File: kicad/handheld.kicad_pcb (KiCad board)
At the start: 4 copper layers, 240 x 76 mm, 95 parts, among them J1 Conn_01x08, J2 61300311121, J3 AVR-PDI-6, J4 UE27AC54100, SW1 HOLD, SW2 PAUSE, SW3 SDROP, SW4 HDROP, SW5 ROTR, SW6 RIGHT, SW7 ROTL, SW8 RIGHT, U1 TFBS4711, U10 DMN601, U11 NSI45015, U12 SN54LV574, U13 P-FET, U14 NSI45015, U15 DMN601, U16 NSI45015, U17 NSI45015, U18 DMN601, U19 P-FET, U2 ATxmega64C3-AU, U20 NSI45015, U21 74HCT595, U22 NSI45015, U23 DMN601, U24 NSI45015, U25 P-FET, U26 NSI45015, U27 DMN601, U28 NSI45015, U29 SN54LV574, U3 P-FET, U30 NSI45015, U31 DMN601, U32 NSI45015, U33 P-FET, U34 NSI45015, U35 DMN601, U36 NSI45015, U37 NSI45015, U38 P-FET, U39 DMN601, U4 LM3671MF-3.3, U40 NSI45015, U41 NSI45015, U42 DMN601, U43 NSI45015, U44 SN54LV574, U45 74HCT595, U46 P-FET, U47 NSI45015, U48 DMN601, U49 NSI45015, U5 NSI45015, U50 NSI45015, U51 DMN601, U52 P-FET, U53 NSI45015, U6 P-FET, U7 DMN601, U8 NSI45015, U9 NSI45015

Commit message: First stab at constant current drivers
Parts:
- moved U9 232.2 mm to (122.4, 117.6), turned to 180 degrees
- moved U5 229.1 mm to (122.4, 120.6), turned to 180 degrees
- moved U17 226.7 mm to (122.4, 111.6), turned to 180 degrees
- moved U8 221.2 mm to (133.4, 120.6), turned to 180 degrees
- moved U16 206.8 mm to (133.4, 114.6), turned to 180 degrees
- moved U11 205.5 mm to (133.4, 117.6), turned to 180 degrees
- moved U20 204.5 mm to (133.4, 111.6), turned to 180 degrees
- moved U14 195.4 mm to (122.4, 114.6), turned to 180 degrees
- moved C7 190.2 mm to (149.5, 128.3), turned to 180 degrees
- moved C10 187.7 mm to (192.6, 90.3), turned to 180 degrees
- moved C8 155.1 mm to (192.5, 128.3), turned to 180 degrees
- moved U36 147.0 mm to (193.4, 151.6), turned to 180 degrees
- moved U24 140.3 mm to (210.0, 161.3), turned to 180 degrees
- moved U30 128.6 mm to (229.1, 161.3), turned to 180 degrees
- moved U22 127.4 mm to (203.7, 161.3), turned to 180 degrees
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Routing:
- net /Matrix Driver/COL3: track 0.00 -> 63.2 mm, vias 0 -> 1
- net /Matrix Driver/COL5: track 0.00 -> 61.6 mm, vias 0 -> 1
- net /Matrix Driver/COL1: track 0.00 -> 61.4 mm, vias 0 -> 1
- net /Matrix Driver/COL0: track 0.00 -> 60.8 mm, vias 0 -> 1
- net /Matrix Driver/COL6: track 0.00 -> 59.6 mm, vias 0 -> 1
- net /Matrix Driver/COL2: track 0.00 -> 48.3 mm, vias 0 -> 1
- net /Matrix Driver/COL4: track 0.00 -> 43.4 mm, vias 0 -> 1
- net /Matrix Driver/COL7: track 0.00 -> 34.9 mm, vias 0 -> 1
- net Net-(U5-Pad1): track 0.00 -> 22.3 mm
- net Net-(U10-Pad6): track 0.00 -> 20.1 mm
- net Net-(U17-Pad1): track 0.00 -> 19.4 mm
- net Net-(U14-Pad1): track 0.00 -> 19.1 mm
- net /Matrix Driver/ROW9: track 97.6 -> 114.2 mm, vias 2 -> 3
- net Net-(U39-Pad2): track 0.00 -> 13.4 mm
- net Net-(U42-Pad2): track 0.00 -> 12.6 mm
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
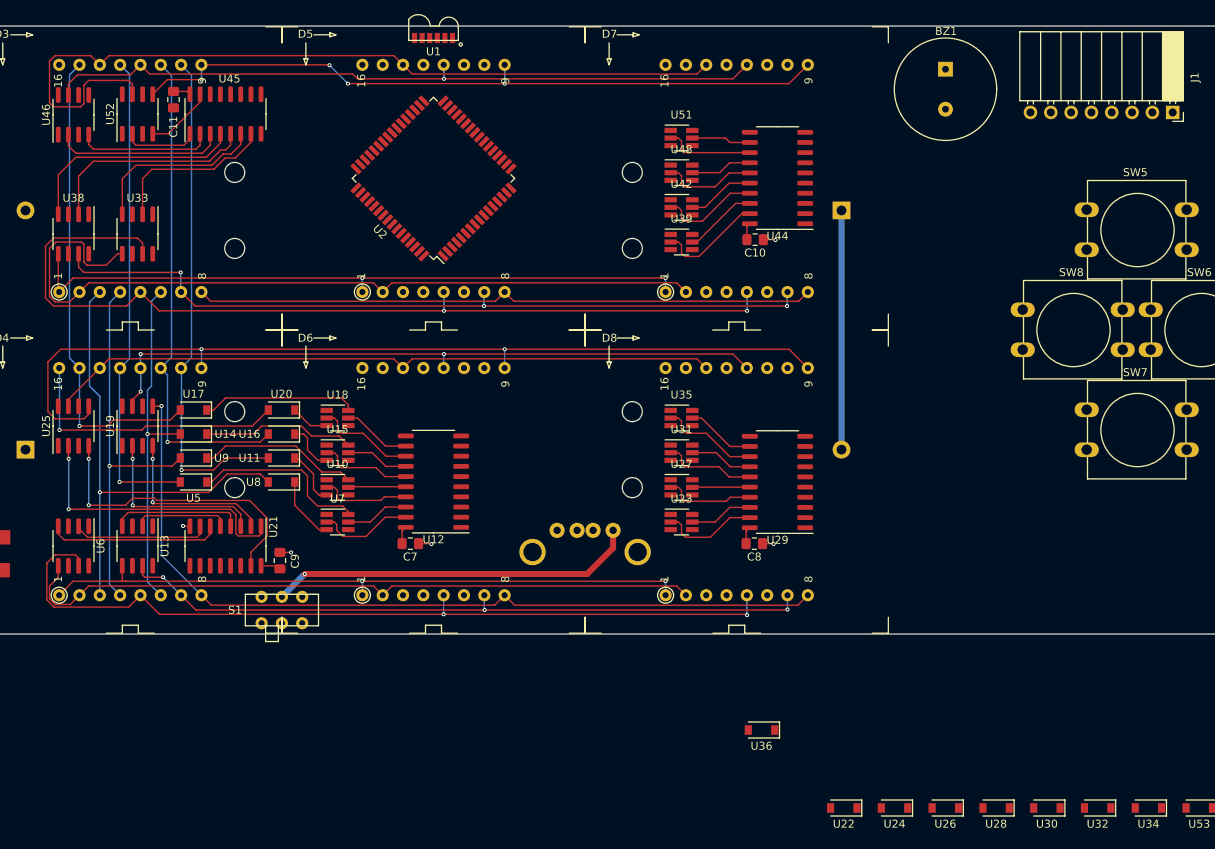
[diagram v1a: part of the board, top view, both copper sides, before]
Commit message: Adds more constant current drivers
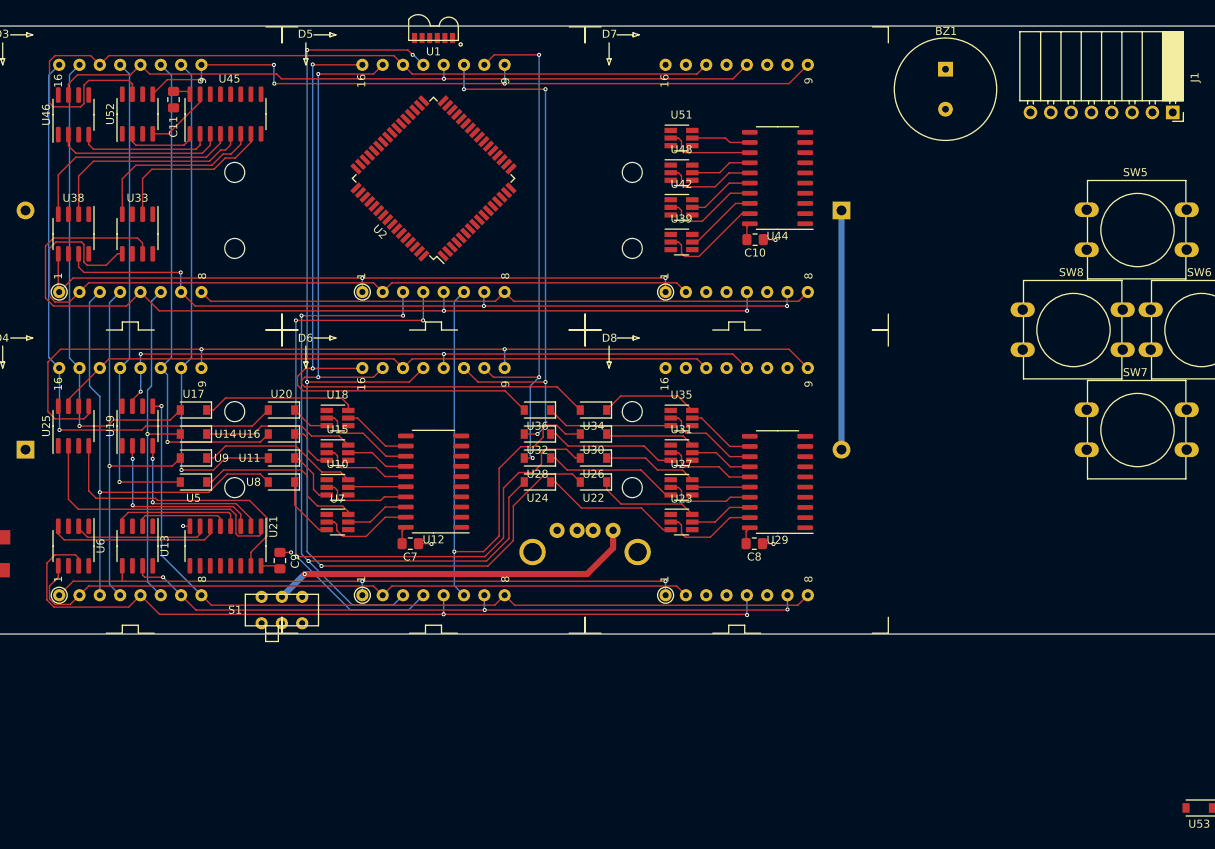
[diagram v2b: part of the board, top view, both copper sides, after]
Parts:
- moved U34 85.4 mm to (172.4, 111.6)
- moved U32 84.2 mm to (165.4, 114.6)
- moved U30 73.5 mm to (172.4, 114.6)
- moved U28 72.1 mm to (165.4, 117.6)
- moved U26 62.0 mm to (172.4, 117.6)
- moved U24 60.4 mm to (165.4, 120.6)
- moved U22 51.4 mm to (172.4, 120.6)
- moved U36 48.8 mm to (165.4, 111.6)
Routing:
- net /Matrix Driver/COL8: track 0.00 -> 135.9 mm, vias 0 -> 4
- net /Matrix Driver/COL10: track 0.00 -> 114.3 mm, vias 0 -> 3
- net /Matrix Driver/COL9: track 0.00 -> 95.4 mm, vias 0 -> 3
- net /Matrix Driver/COL14: track 0.00 -> 93.8 mm, vias 0 -> 2
- net /Matrix Driver/COL15: track 0.00 -> 83.5 mm, vias 0 -> 2
- net /Matrix Driver/COL13: track 0.00 -> 69.3 mm, vias 0 -> 4
- net /Matrix Driver/COL12: track 0.00 -> 67.3 mm, vias 0 -> 1
- net /Matrix Driver/COL11: track 0.00 -> 66.7 mm, vias 0 -> 3
- net /Matrix Driver/COL7: track 34.9 -> 73.9 mm
- net Net-(U23-Pad3): track 0.00 -> 17.5 mm
- net Net-(U27-Pad3): track 0.00 -> 16.9 mm
- net Net-(U31-Pad3): track 0.00 -> 16.4 mm
- net Net-(U35-Pad3): track 0.00 -> 15.8 mm
- net Net-(U22-Pad1): track 0.00 -> 12.9 mm
- net Net-(U34-Pad1): track 0.00 -> 12.2 mm
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
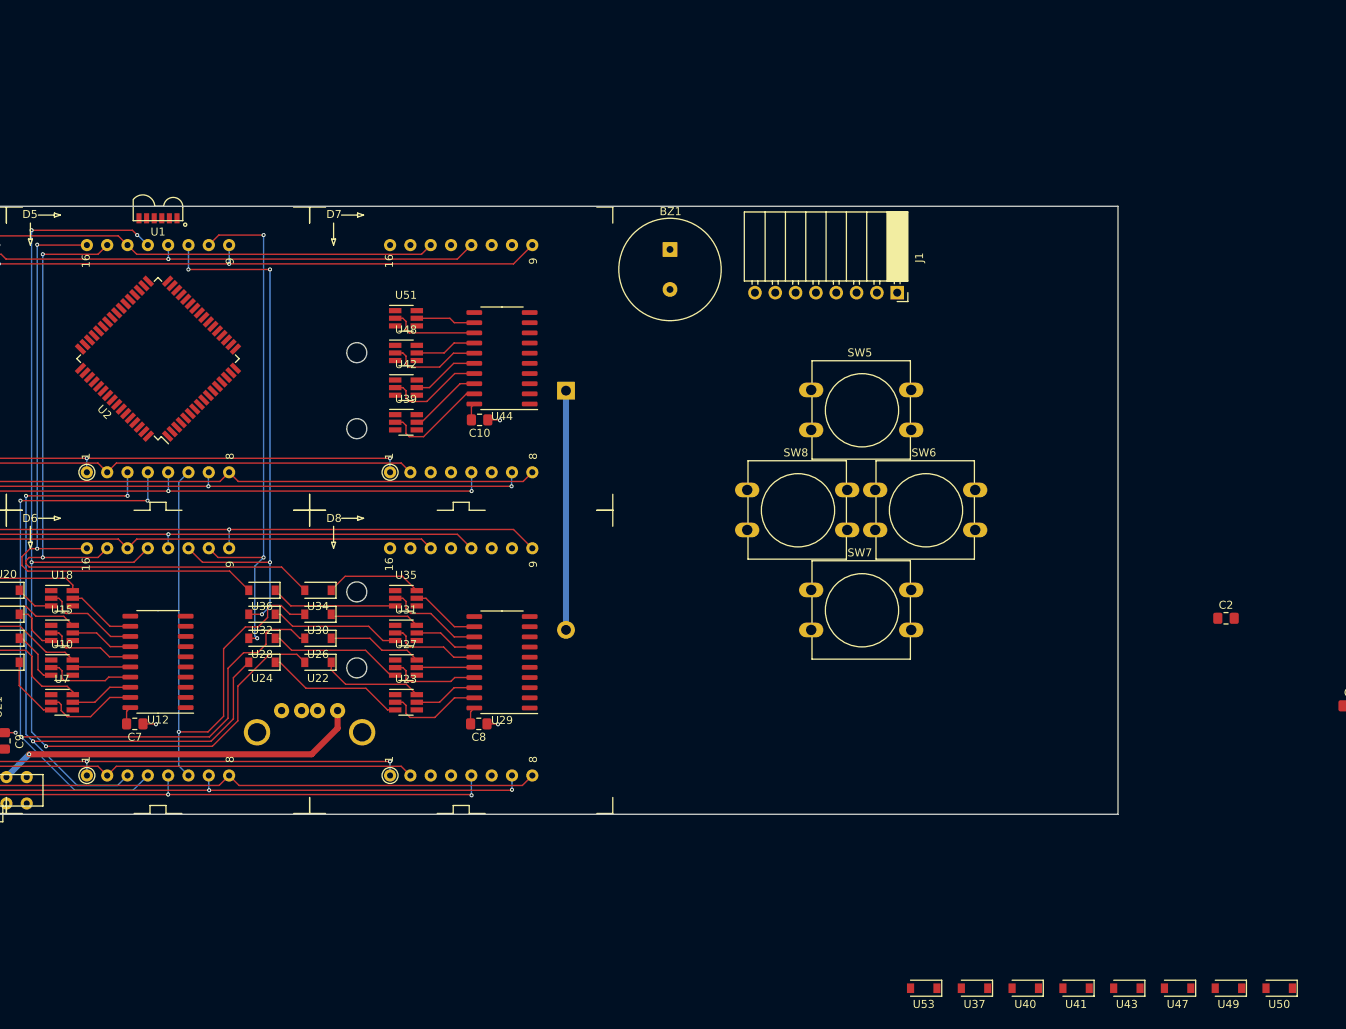
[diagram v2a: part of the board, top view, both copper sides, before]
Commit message: Adds more column circuitry
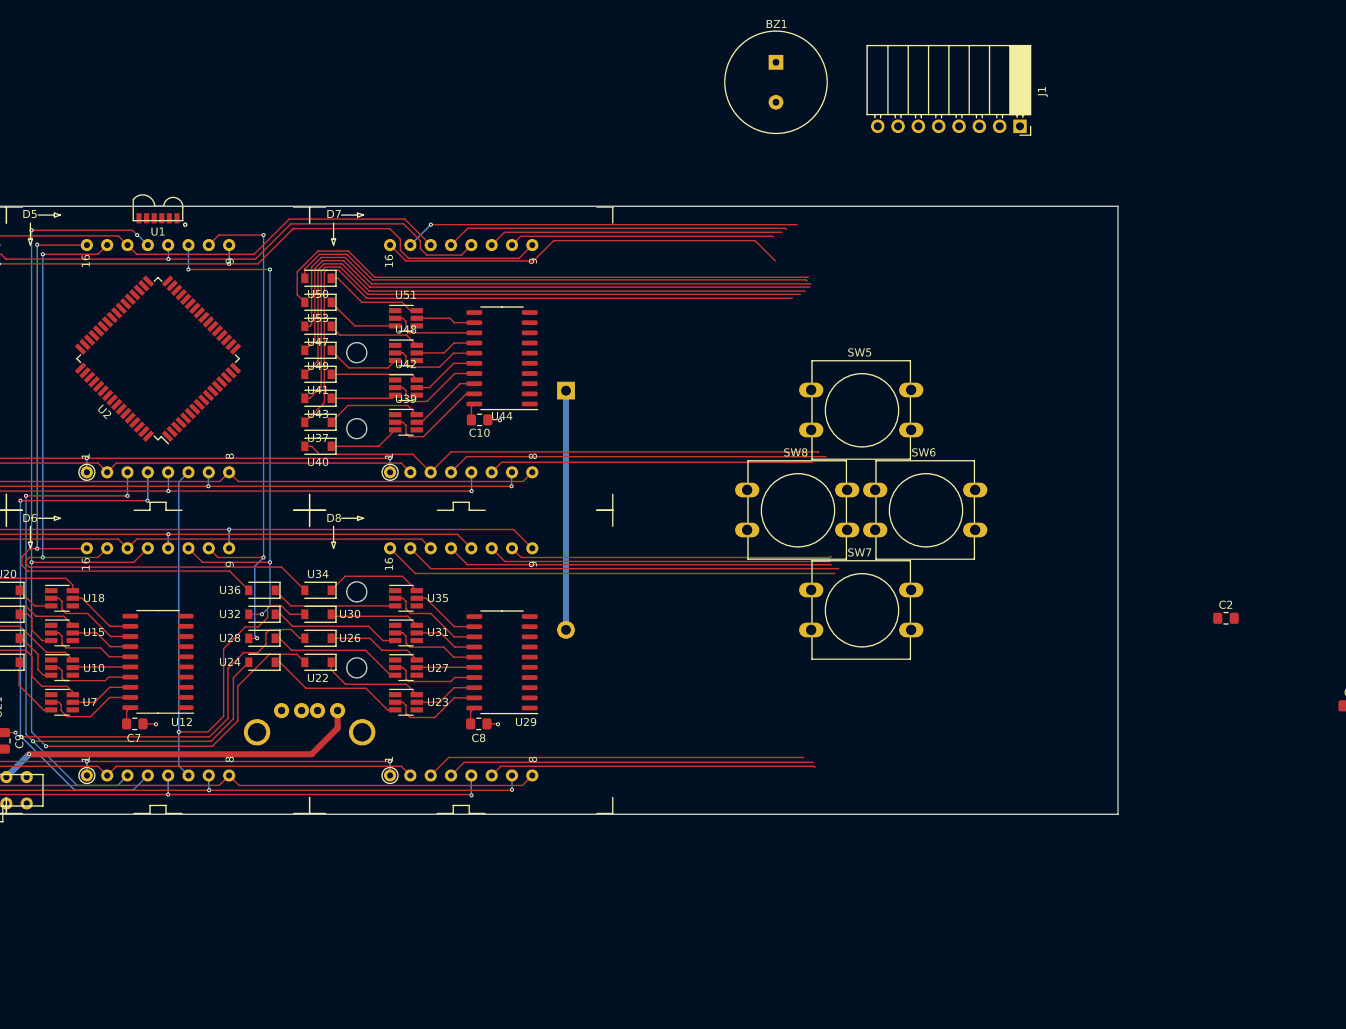
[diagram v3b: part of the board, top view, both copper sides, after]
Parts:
- moved U50 149.4 mm to (172.4, 72.6)
- moved U49 139.0 mm to (172.4, 81.6)
- moved U47 135.6 mm to (172.4, 78.6)
- moved U43 125.1 mm to (172.4, 87.6)
- moved U41 121.9 mm to (172.4, 84.6)
- moved U53 114.4 mm to (172.4, 75.6)
- moved U40 111.4 mm to (172.4, 93.6)
- moved U37 108.3 mm to (172.4, 90.6)
- moved BZ1 26.9 mm to (229.7, 45.6)
- moved J1 25.9 mm to (260.1, 53.6)
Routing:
- net /Matrix Driver/COL23: track 0.00 -> 178.5 mm
- net /Matrix Driver/COL16: track 0.00 -> 171.1 mm
- net /Matrix Driver/COL22: track 0.00 -> 170.1 mm, vias 0 -> 1
- net /Matrix Driver/COL18: track 0.00 -> 170.0 mm
- net /Matrix Driver/COL21: track 0.00 -> 154.3 mm
- net /Matrix Driver/COL20: track 0.00 -> 154.0 mm
- net /Matrix Driver/COL19: track 0.00 -> 152.2 mm
- net /Matrix Driver/COL17: track 0.00 -> 114.2 mm
- net Net-(U50-Pad1): track 0.00 -> 12.4 mm
- net Net-(U37-Pad1): track 0.00 -> 12.0 mm
- net Net-(U47-Pad1): track 0.00 -> 11.7 mm
- net Net-(U41-Pad1): track 0.00 -> 11.0 mm
- net Net-(U48-Pad3): track 0.00 -> 9.29 mm
- net Net-(U51-Pad3): track 0.00 -> 9.22 mm
- net Net-(U39-Pad3): track 0.00 -> 8.85 mm
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
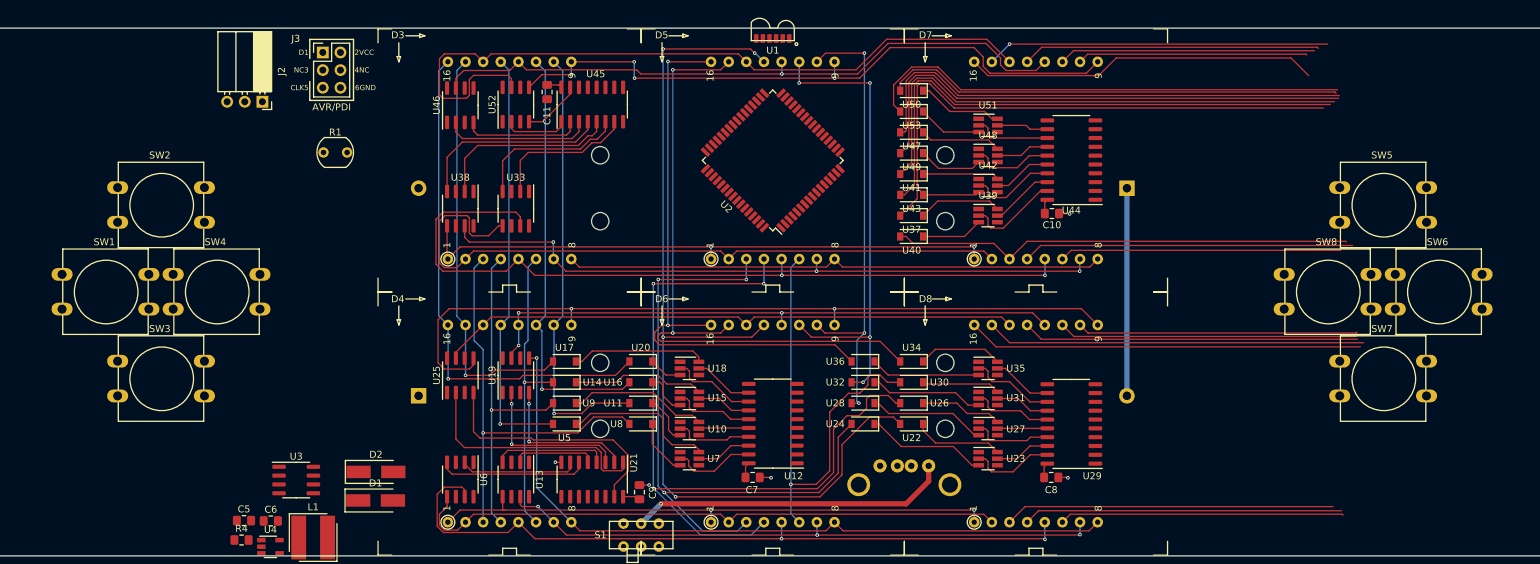
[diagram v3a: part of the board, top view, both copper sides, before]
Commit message: Wires up USB and buttons
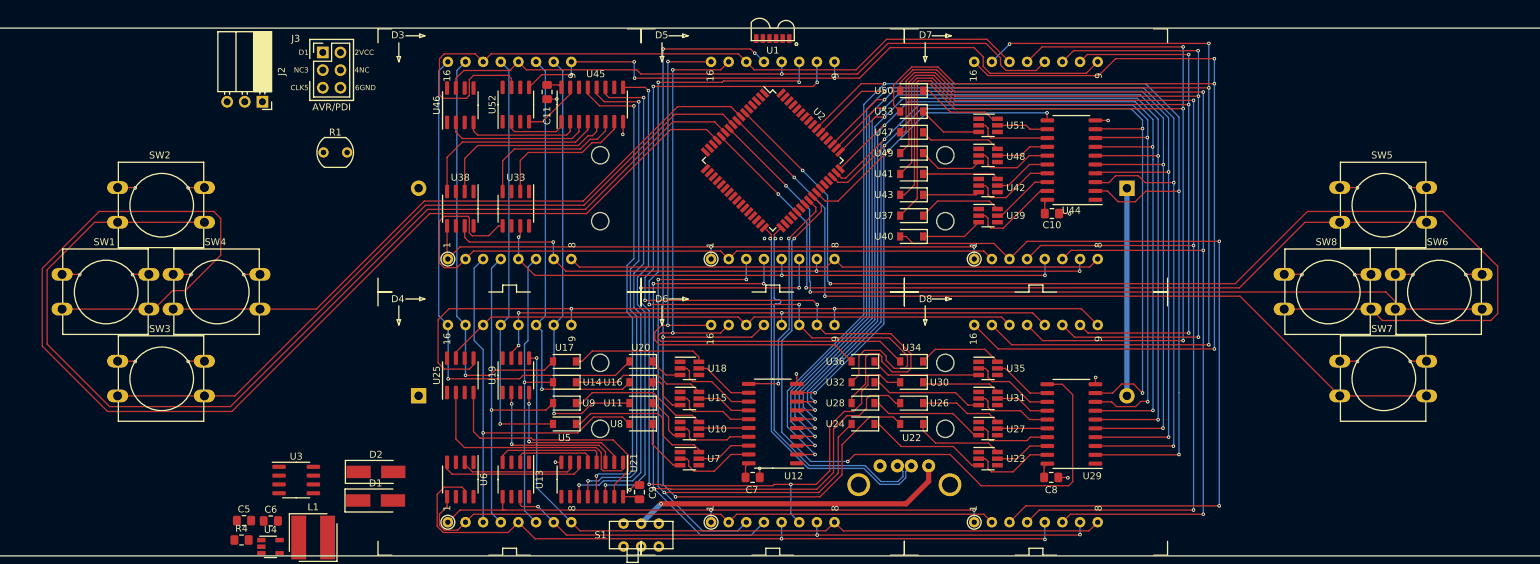
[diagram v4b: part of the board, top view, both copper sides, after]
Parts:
- turned U2 to 315 degrees
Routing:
- net /D7: track 0.00 -> 194.4 mm, vias 0 -> 4
- net Net-(SW1-Pad2): track 0.00 -> 190.6 mm
- net /D6: track 0.00 -> 186.8 mm, vias 0 -> 4
- net /D5: track 0.00 -> 178.2 mm, vias 0 -> 4
- net Net-(SW8-Pad2): track 0.00 -> 172.1 mm, vias 0 -> 2
- net /D4: track 0.00 -> 170.8 mm, vias 0 -> 4
- net /D3: track 0.00 -> 163.5 mm, vias 0 -> 4
- net /D2: track 0.00 -> 157.5 mm, vias 0 -> 4
- net Net-(SW2-Pad2): track 0.00 -> 155.2 mm
- net /D1: track 0.00 -> 151.8 mm, vias 0 -> 4
- net /D0: track 0.00 -> 146.4 mm, vias 0 -> 4
- net Net-(SW6-Pad2): track 0.00 -> 126.8 mm, vias 0 -> 2
- net Net-(SW7-Pad2): track 0.00 -> 123.2 mm, vias 0 -> 2
- net Net-(SW5-Pad2): track 0.00 -> 120.2 mm, vias 0 -> 2
- net Net-(SW3-Pad2): track 0.00 -> 106.0 mm
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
